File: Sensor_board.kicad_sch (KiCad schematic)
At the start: 20 parts, among them U1001 LP5907MFX-1.8, U903 LP5907MFX-3.3

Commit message: change 10u cap from 0805 to 0402
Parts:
- C1005: footprint Capacitor_SMD:C_0805_2012Metric_Pad1.18x1.45mm_HandSolder -> Capacitor_SMD:C_0402_1005Metric; MPN C0805C106K9PACTU -> GRM155R60J106ME05D; Mfr. KEMET -> Murata
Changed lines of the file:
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@@
       (effects (font (size 1.27 1.27)) (justify left))
     )
-    (property "Footprint" "Capacitor_SMD:C_0805_2012Metric_Pad1.18x1.45mm_HandSolder" (at 184.15 102.235 0)
+    (property "Footprint" "Capacitor_SMD:C_0402_1005Metric" (at 184.15 102.235 0)
       (effects (font (size 1.27 1.27)) hide)
     )
@@
       (effects (font (size 1.27 1.27)) hide)
     )
-    (property "MPN" "C0805C106K9PACTU" (at 184.15 102.235 0)
+    (property "MPN" "GRM155R60J106ME05D" (at 184.15 102.235 0)
       (effects (font (size 1.27 1.27)) hide)
     )
-    (property "Mfr." "KEMET" (at 184.15 102.235 0)
+    (property "Mfr." "Murata" (at 184.15 102.235 0)
       (effects (font (size 1.27 1.27)) hide)
     )

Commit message: replace passives with 0402
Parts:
- C1001, C1003, C1006, C1007, C1008: footprint Capacitor_SMD:C_0603_1608Metric_Pad1.08x0.95mm_HandSolder -> Capacitor_SMD:C_0402_1005Metric; MPN C0603C105K8RACTU -> C0402C105K9PACTU
- FB904: footprint Inductor_SMD:L_0603_1608Metric_Pad1.05x0.95mm_HandSolder -> Inductor_SMD:L_0402_1005Metric; MPN BLM18KG101TZ1D -> BLM15HD102SN1D
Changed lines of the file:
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@@
       (effects (font (size 1.27 1.27)) (justify left))
     )
-    (property "Footprint" "Capacitor_SMD:C_0603_1608Metric_Pad1.08x0.95mm_HandSolder" (at 139.7 102.235 0)
+    (property "Footprint" "Capacitor_SMD:C_0402_1005Metric" (at 139.7 102.235 0)
       (effects (font (size 1.27 1.27)) hide)
     )
@@
       (effects (font (size 1.27 1.27)) hide)
     )
-    (property "MPN" "C0603C105K8RACTU" (at 139.7 102.235 0)
+    (property "MPN" "C0402C105K9PACTU" (at 139.7 102.235 0)
       (effects (font (size 1.27 1.27)) hide)
     )
@@
       (effects (font (size 1.27 1.27)) (justify left))
     )
-    (property "Footprint" "Capacitor_SMD:C_0603_1608Metric_Pad1.08x0.95mm_HandSolder" (at 85.09 102.235 0)
+    (property "Footprint" "Capacitor_SMD:C_0402_1005Metric" (at 85.09 102.235 0)
       (effects (font (size 1.27 1.27)) hide)
     )
@@
       (effects (font (size 1.27 1.27)) hide)
     )
-    (property "MPN" "C0603C105K8RACTU" (at 85.09 102.235 0)
+    (property "MPN" "C0402C105K9PACTU" (at 85.09 102.235 0)
       (effects (font (size 1.27 1.27)) hide)
     )
@@
       (effects (font (size 1.27 1.27)) (justify left))
     )
-    (property "Footprint" "Capacitor_SMD:C_0603_1608Metric_Pad1.08x0.95mm_HandSolder" (at 85.725 135.255 0)
+    (property "Footprint" "Capacitor_SMD:C_0402_1005Metric" (at 85.725 135.255 0)
       (effects (font (size 1.27 1.27)) hide)
     )
@@
       (effects (font (size 1.27 1.27)) hide)
     )
-    (property "MPN" "C0603C105K8RACTU" (at 85.725 135.255 0)
+    (property "MPN" "C0402C105K9PACTU" (at 85.725 135.255 0)
       (effects (font (size 1.27 1.27)) hide)
     )
@@
       (effects (font (size 1.27 1.27)) (justify left))
     )
-    (property "Footprint" "Capacitor_SMD:C_0603_1608Metric_Pad1.08x0.95mm_HandSolder" (at 140.335 135.255 0)
+    (property "Footprint" "Capacitor_SMD:C_0402_1005Metric" (at 140.335 135.255 0)
       (effects (font (size 1.27 1.27)) hide)
     )
@@
       (effects (font (size 1.27 1.27)) hide)
     )
-    (property "MPN" "C0603C105K8RACTU" (at 140.335 135.255 0)
+    (property "MPN" "C0402C105K9PACTU" (at 140.335 135.255 0)
       (effects (font (size 1.27 1.27)) hide)
     )
@@
       (effects (font (size 1.27 1.27)) (justify left))
     )
-    (property "Footprint" "Capacitor_SMD:C_0603_1608Metric_Pad1.08x0.95mm_HandSolder" (at 160.02 102.87 0)
+    (property "Footprint" "Capacitor_SMD:C_0402_1005Metric" (at 160.02 102.87 0)
       (effects (font (size 1.27 1.27)) hide)
     )
@@
       (effects (font (size 1.27 1.27)) hide)
     )
-    (property "MPN" "C0603C105K8RACTU" (at 160.02 102.87 0)
+    (property "MPN" "C0402C105K9PACTU" (at 160.02 102.87 0)
       (effects (font (size 1.27 1.27)) hide)
     )
@@
       (effects (font (size 1.27 1.27)))
     )
-    (property "Footprint" "Inductor_SMD:L_0603_1608Metric_Pad1.05x0.95mm_HandSolder" (at 172.085 98.933 90)
+    (property "Footprint" "Inductor_SMD:L_0402_1005Metric" (at 172.085 98.933 90)
       (effects (font (size 1.27 1.27)) hide)
     )
@@
       (effects (font (size 1.27 1.27)) hide)
     )
-    (property "MPN" "BLM18KG101TZ1D" (at 172.085 97.155 90)
-      (effects (font (size 1.27 1.27)) hide)
-    )
+    (property "MPN" "BLM15HD102SN1D" (at 172.085 97.155 90)
+      (effects (font (size 1.27 1.27)) hide)
+    )

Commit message: (pcb) layout summing out
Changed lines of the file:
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@@
     (effects (font (size 1.27 1.27) (thickness 0.254) bold) (justify left bottom))
+  )
+  (label "SUM_OUT_P" (at 129.54 57.15 0) (fields_autoplaced)
+    (effects (font (size 1.27 1.27)) (justify left bottom))
   )
   (label "VCC_FILT" (at 95.25 93.345 0) (fields_autoplaced)
@@
     (effects (font (size 1.27 1.27)) (justify left bottom))
   )
+  (label "SUM_OUT_N" (at 129.54 62.23 0) (fields_autoplaced)
+    (effects (font (size 1.27 1.27)) (justify left bottom))
+  )

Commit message: (sch) add VCM decoupling
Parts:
- removed C1008: 1u, Capacitor_SMD:C_0402_1005Metric, symbol Device:C_Small
- removed CB1003, CB1004: 100n, Capacitor_SMD:C_0402_1005Metric, symbol Device:C_Small
- added C1002: 10u, Capacitor_SMD:C_0402_1005Metric, symbol Device:C_Small
- added C1004: 1u, Capacitor_SMD:C_0402_1005Metric, symbol Device:C_Small
- C1001: value 1u -> 10u; MPN C0402C105K9PACTU -> GRM155R60J106ME05D; Mfr. KEMET -> Murata
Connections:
- net +1V8: now also C1004.1
- net +3.3V: now also C1002.1
- net GND: now also C1002.2, C1004.2

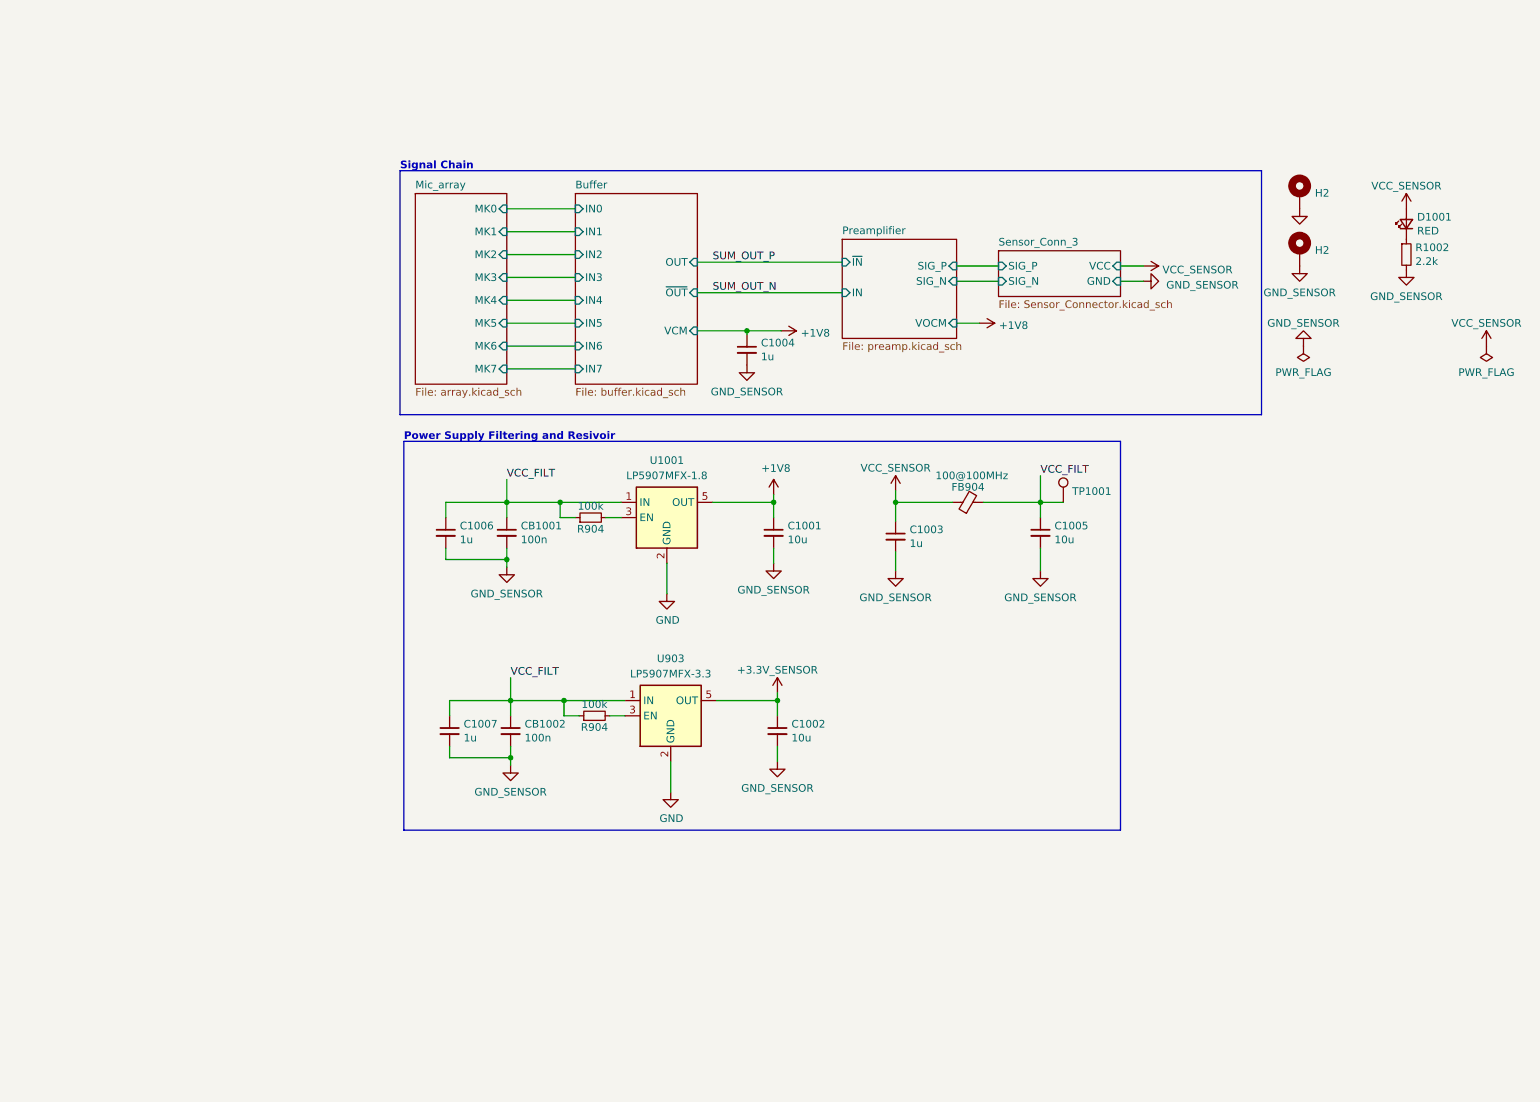
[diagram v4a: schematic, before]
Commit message: (sch) fix diff to single-end conn.
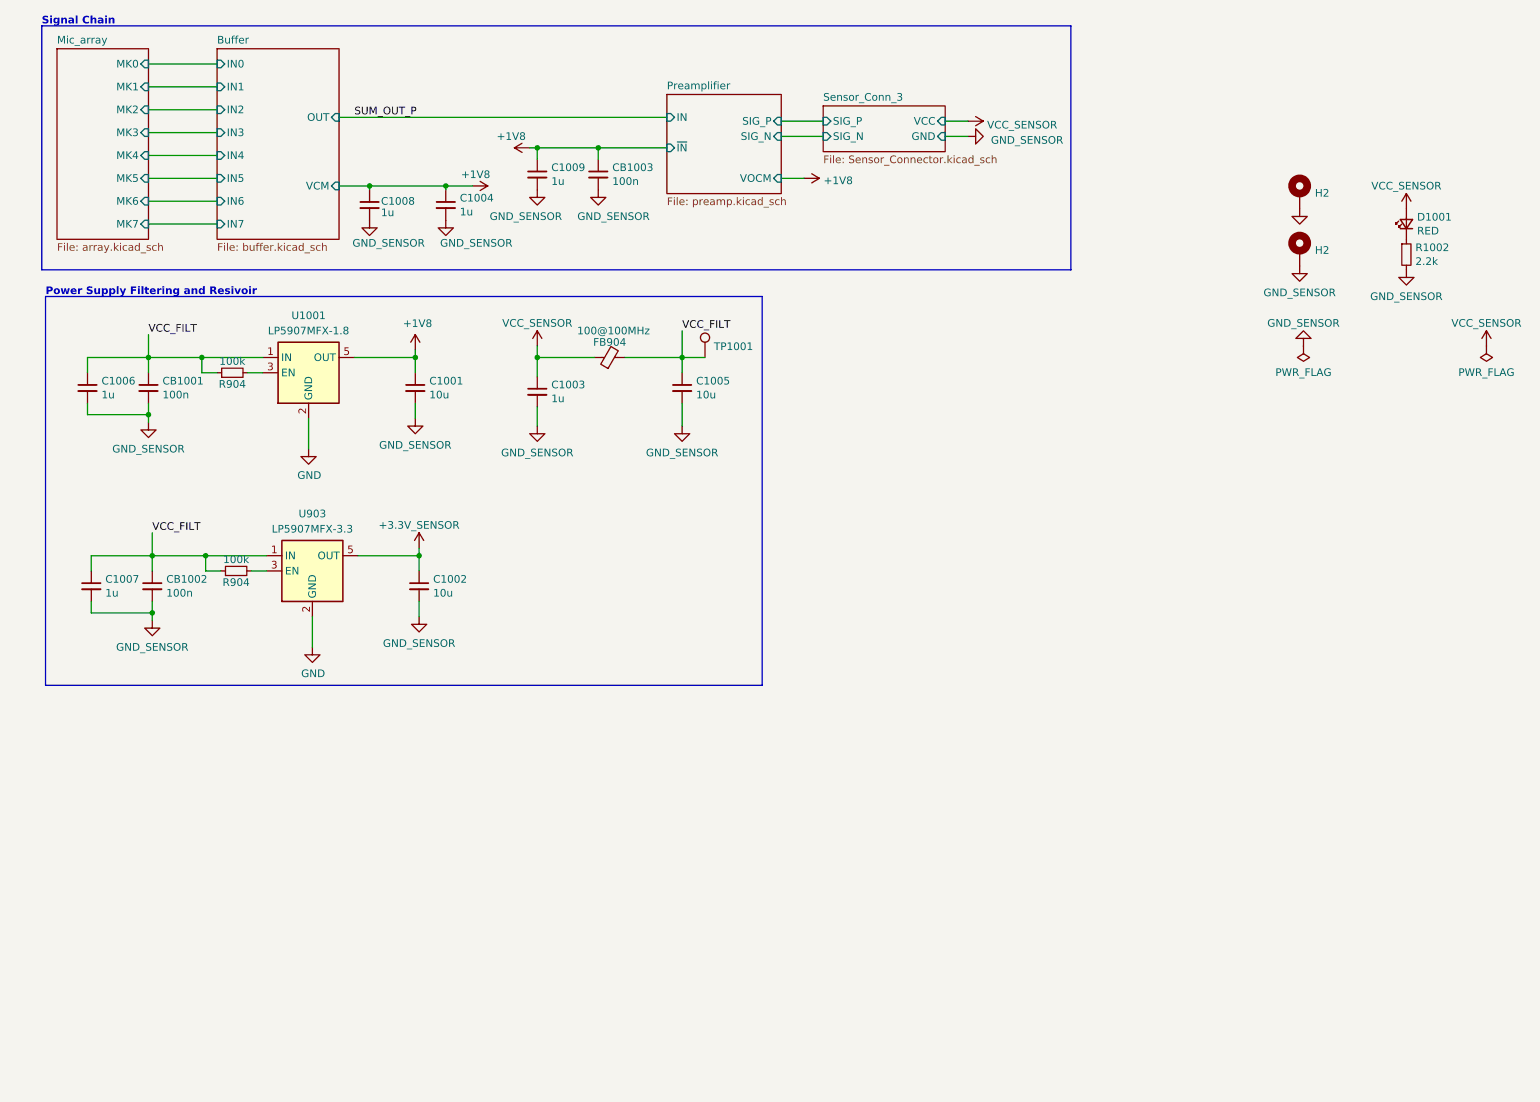
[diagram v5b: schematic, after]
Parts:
- added C1008, C1009: 1u, Capacitor_SMD:C_0402_1005Metric, symbol Device:C_Small
- added CB1003: 100n, Capacitor_SMD:C_0402_1005Metric, symbol Device:C_Small
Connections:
- net +1V8: now also C1008.1, C1009.1, CB1003.1
- net GND: now also C1008.2, C1009.2, CB1003.2
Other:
- sheet Buffer ports: added none; removed ~{OUT}
- moved on the sheet: C1001, C1002, C1003, C1004, C1005, C1006, C1007, CB1001, CB1002, FB904, R904, TP1001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

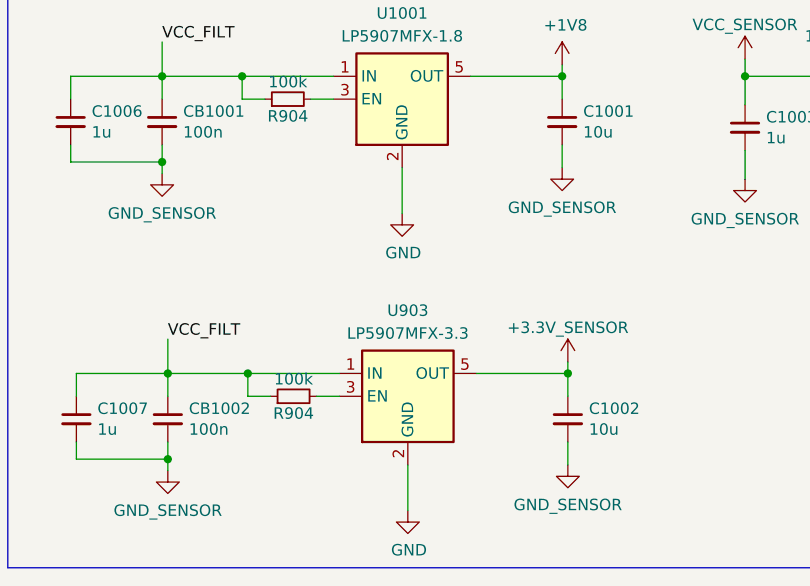
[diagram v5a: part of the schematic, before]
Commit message: (sch) fix board seperate net labels
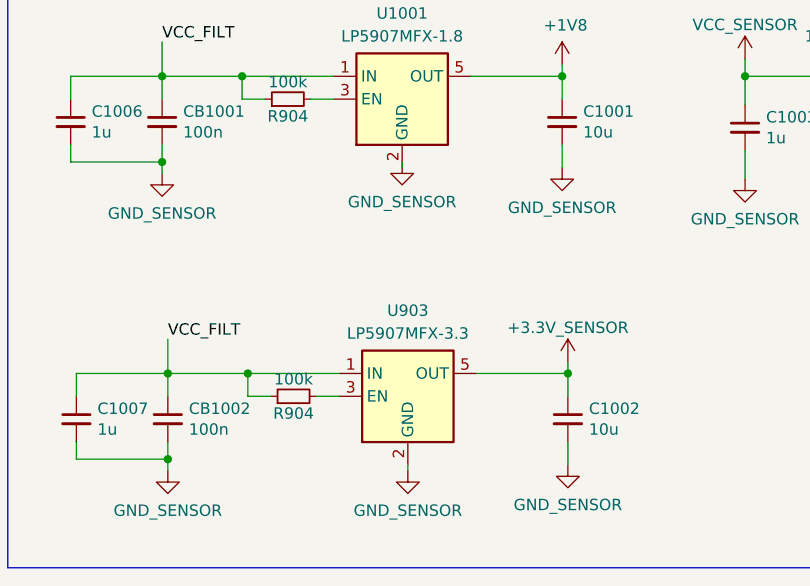
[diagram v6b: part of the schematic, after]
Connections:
- net +3.3V renamed VCC_SENSOR
- net VCC_SENSOR: no longer C1002.1, U903.5 (OUT)
- net GND renamed GND_SENSOR
- new net +3.3V_SENSOR: C1002.1, U903.5 (OUT)
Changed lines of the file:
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@@
     (stroke (width 0) (type default))
   )
-  (wire (pts (xy 62.865 116.205) (xy 62.865 121.285))
+  (wire (pts (xy 62.865 116.205) (xy 62.865 116.84))
     (stroke (width 0) (type default))
   )
@@
     (stroke (width 0) (type default))
   )
-  (wire (pts (xy 62.23 83.185) (xy 62.23 88.265))
+  (wire (pts (xy 62.23 83.185) (xy 62.23 82.55))
     (stroke (width 0) (type default))
   )
@@
     )
   )
-  (symbol (lib_id "power:GND") (at 62.23 88.265 0) (unit 1)
-    (in_bom yes) (on_board yes) (dnp no)
-    (property "Reference" "#PWR01004" (at 62.23 94.615 0)
-      (effects (font (size 1.27 1.27)) hide)
-    )
-    (property "Value" "GND" (at 62.357 92.6592 0)
-      (effects (font (size 1.27 1.27)))
-    )
-    (property "Footprint" "" (at 62.23 88.265 0)
-      (effects (font (size 1.27 1.27)) hide)
-    )
-    (property "Datasheet" "" (at 62.23 88.265 0)
-      (effects (font (size 1.27 1.27)) hide)
-    )
-    (pin "1")
-    (instances
-      (project "kleinvoet"
-        (path "/4185c36c-c66e-4dbd-be5d-841e551f4885/b53619ea-788f-4bc9-9946-594014d7d22c"
-          (reference "#PWR01004") (unit 1)
-        )
-      )
-      (project "Sensor_Board"
-        (path "/7578b70c-b222-4cd3-b4ed-e0af47d4ab95"
-          (reference "#PWR05") (unit 1)
-        )
-      )
-    )
-  )
   (symbol (lib_id "Device:C_Small") (at 35.56 78.105 0) (unit 1)
     (in_bom yes) (on_board yes) (dnp no)
@@
         (path "/4185c36c-c66e-4dbd-be5d-841e551f4885/b53619ea-788f-4bc9-9946-594014d7d22c"
           (reference "#PWR01025") (unit 1)
-        )
-      )
-    )
-  )
-  (symbol (lib_id "power:GND") (at 62.865 121.285 0) (unit 1)
-    (in_bom yes) (on_board yes) (dnp no)
-    (property "Reference" "#PWR01003" (at 62.865 127.635 0)
-      (effects (font (size 1.27 1.27)) hide)
-    )
-    (property "Value" "GND" (at 62.992 125.6792 0)
-      (effects (font (size 1.27 1.27)))
-    )
-    (property "Footprint" "" (at 62.865 121.285 0)
-      (effects (font (size 1.27 1.27)) hide)
-    )
-    (property "Datasheet" "" (at 62.865 121.285 0)
-      (effects (font (size 1.27 1.27)) hide)
-    )
-    (pin "1")
-    (instances
-      (project "kleinvoet"
-        (path "/4185c36c-c66e-4dbd-be5d-841e551f4885/b53619ea-788f-4bc9-9946-594014d7d22c"
-          (reference "#PWR01003") (unit 1)
-        )
-      )
-      (project "Sensor_Board"
-        (path "/7578b70c-b222-4cd3-b4ed-e0af47d4ab95"
-          (reference "#PWR05") (unit 1)
         )
       )
@@
         )
       )
+    )
+  )
+  (symbol (lib_id "grootvoet:GND_SENSOR") (at 62.865 116.84 0) (unit 1)
+    (in_bom yes) (on_board yes) (dnp no) (fields_autoplaced)
+    (property "Reference" "#PWR09" (at 62.865 123.19 0)
+      (effects (font (size 1.27 1.27)) hide)
+    )
+    (property "Value" "GND_SENSOR" (at 62.865 121.285 0)
+      (effects (font (size 1.27 1.27)))
+    )
+    (property "Footprint" "" (at 62.865 116.84 0)
+      (effects (font (size 1.27 1.27)) hide)
+    )
+    (property "Datasheet" "" (at 62.865 116.84 0)
+      (effects (font (size 1.27 1.27)) hide)
+    )
+    (pin "1")
+    (instances
+      (project "kleinvoet"
+        (path "/4185c36c-c66e-4dbd-be5d-841e551f4885/b53619ea-788f-4bc9-9946-594014d7d22c"
+          (reference "#PWR09") (unit 1)
+        )
+      )
+    )
+  )
+  (symbol (lib_id "grootvoet:GND_SENSOR") (at 62.23 82.55 0) (unit 1)
+    (in_bom yes) (on_board yes) (dnp no) (fields_autoplaced)
+    (property "Reference" "#PWR08" (at 62.23 88.9 0)
+      (effects (font (size 1.27 1.27)) hide)
+    )
+    (property "Value" "GND_SENSOR" (at 62.23 86.995 0)
+      (effects (font (size 1.27 1.27)))
+    )
+    (property "Footprint" "" (at 62.23 82.55 0)
+      (effects (font (size 1.27 1.27)) hide)
+    )
+    (property "Datasheet" "" (at 62.23 82.55 0)
+      (effects (font (size 1.27 1.27)) hide)
+    )
+    (pin "1")
+    (instances
+      (project "kleinvoet"
+        (path "/4185c36c-c66e-4dbd-be5d-841e551f4885/b53619ea-788f-4bc9-9946-594014d7d22c"
+          (reference "#PWR08") (unit 1)
+        )
+      )

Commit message: (sch) run DRC
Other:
- moved on the sheet: D1001, H2, R1002

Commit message: (sch) consoldate BOM
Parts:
- TP1001: MPN ICS-40300 -> (none); Mfr. TDK InvenSense -> (none)
- U1001: MPN (none) -> LP5907MFX-1.8/NOPB; Mfr. (none) -> Texas Instruments
- U903: MPN (none) -> LP5907MFX-3.3/NOPB; Mfr. (none) -> Texas Instruments
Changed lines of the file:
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@@
       (effects (font (size 1.27 1.27)) hide)
     )
-    (property "Mfr." "TDK InvenSense" (at 128.27 73.025 0)
-      (effects (font (size 1.27 1.27)) hide)
-    )
-    (property "MPN" "ICS-40300" (at 128.27 73.025 0)
+    (property "Mfr." "" (at 128.27 73.025 0)
+      (effects (font (size 1.27 1.27)) hide)
+    )
+    (property "MPN" "" (at 128.27 73.025 0)
       (effects (font (size 1.27 1.27)) hide)
     )
@@
     )
     (property "Datasheet" "http://www.ti.com/lit/ds/symlink/lp5907.pdf" (at 62.865 95.885 0)
+      (effects (font (size 1.27 1.27)) hide)
+    )
+    (property "MPN" "LP5907MFX-3.3/NOPB" (at 62.865 108.585 0)
+      (effects (font (size 1.27 1.27)) hide)
+    )
+    (property "Mfr." "Texas Instruments" (at 62.865 108.585 0)
       (effects (font (size 1.27 1.27)) hide)
     )
@@
       (effects (font (size 1.27 1.27)) hide)
     )
+    (property "MPN" "LP5907MFX-1.8/NOPB" (at 62.23 75.565 0)
+      (effects (font (size 1.27 1.27)) hide)
+    )
+    (property "Mfr." "Texas Instruments" (at 62.23 75.565 0)
+      (effects (font (size 1.27 1.27)) hide)
+    )
